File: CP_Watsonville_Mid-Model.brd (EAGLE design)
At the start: 100 x 100 mm, 12 parts

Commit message: Aligned between boards
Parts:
- moved CON1 3.81 mm to (88.9, 21.6)
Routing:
- net DAAT: track 91.9 -> 96.0 mm
- net 1SAAT: track 79.9 -> 83.9 mm
- net 2SAAT: track 68.9 -> 72.9 mm
- net 3SAAT: track 58.1 -> 62.1 mm
- net 4SAAT: track 47.1 -> 51.1 mm
- net VCC: track 152.0 -> 155.8 mm
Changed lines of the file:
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@@
 <layer number="19" name="Unrouted" color="6" fill="1" visible="no" active="yes"/>
 <layer number="20" name="Dimension" color="15" fill="1" visible="yes" active="yes"/>
-<layer number="21" name="tPlace" color="7" fill="1" visible="yes" active="yes"/>
+<layer number="21" name="tPlace" color="39" fill="1" visible="yes" active="yes"/>
 <layer number="22" name="bPlace" color="7" fill="1" visible="no" active="yes"/>
 <layer number="23" name="tOrigins" color="15" fill="1" visible="no" active="yes"/>
@@
 <text x="48.514" y="41.783" size="1.27" layer="21" font="vector" ratio="10">3SAAT</text>
 <text x="48.514" y="29.083" size="1.27" layer="21" font="vector" ratio="10">4SAAT</text>
-<text x="76.327" y="23.241" size="1.016" layer="21" font="vector" ratio="10">John Plocher</text>
-<text x="77.597" y="20.701" size="1.016" layer="21" font="vector" ratio="10">2020.10</text>
+<text x="84.709" y="12.192" size="1.016" layer="22" font="vector" ratio="10" rot="MR90">John Plocher</text>
+<text x="82.169" y="13.462" size="1.016" layer="22" font="vector" ratio="10" rot="MR90">2020.10</text>
 <text x="92.456" y="82.042" size="5.08" layer="22" font="vector" ratio="15" rot="MR0">SPCoast.com
 CP Watsonville Middle</text>
 <text x="85.09" y="48.26" size="5.08" layer="22" font="vector" ratio="15" rot="MR0">Model Board
 Field Unit repeater</text>
-<text x="91.44" y="7.62" size="2.54" layer="22" font="vector" ratio="10" rot="MR0">V1.0 2020.10</text>
+<text x="60.96" y="2.54" size="2.54" layer="22" font="vector" ratio="10" rot="MR0">V1.0 2020.10</text>
 <text x="5.08" y="77.47" size="2.54" layer="22" font="vector" ratio="10" rot="MR270">Model Railroading is Fun!</text>
 <text x="97.79" y="90.17" size="2.54" layer="22" font="vector" ratio="10" rot="MR270">Made in the PCR, Coast Division, NMRA</text>
@@
 <wire x1="97.79" y1="33.02" x2="95.25" y2="33.02" width="0.6096" layer="21"/>
 <wire x1="1.27" y1="83.82" x2="3.81" y2="83.82" width="0.6096" layer="21"/>
-<circle x="88.9" y="25.4" radius="1.79605" width="0.4064" layer="21"/>
+<circle x="88.9" y="21.59" radius="1.79605" width="0.4064" layer="22"/>
 </plain>
 <attributes>
@@
 <attribute name="VALUE" x="52.07" y="34.925" size="0.3048" layer="27" font="vector" rot="R180"/>
 </element>
-<element name="CON1" library="SPCoast" package="1X06_LOCK" value="" x="88.9" y="25.4" rot="R270"/>
+<element name="CON1" library="SPCoast" package="1X06_LOCK" value="" x="88.9" y="21.59" rot="R270"/>
 </elements>
 <signals>
@@
 <wire x1="49.9" y1="58.42" x2="49.9" y2="45.72" width="0.3048" layer="1"/>
 <wire x1="49.9" y1="45.72" x2="49.9" y2="33.02" width="0.3048" layer="1"/>
-<wire x1="88.9" y1="25.4" x2="88.9" y2="85.09" width="0.4064" layer="1"/>
+<wire x1="88.9" y1="21.59" x2="88.9" y2="85.09" width="0.4064" layer="1"/>
 <wire x1="88.9" y1="85.09" x2="87.63" y2="86.36" width="0.4064" layer="1"/>
 <wire x1="87.63" y1="86.36" x2="50.8" y2="86.36" width="0.4064" layer="1"/>
@@
 <wire x1="55.36" y1="45.72" x2="78.74" y2="45.72" width="0.3048" layer="1"/>
 <wire x1="78.74" y1="45.72" x2="80.01" y2="44.45" width="0.3048" layer="1"/>
-<wire x1="80.01" y1="44.45" x2="80.01" y2="24.13" width="0.3048" layer="1"/>
-<wire x1="80.01" y1="24.13" x2="88.9" y2="15.24" width="0.3048" layer="1"/>
+<wire x1="80.01" y1="44.45" x2="80.01" y2="19.685" width="0.3048" layer="1"/>
+<wire x1="80.01" y1="19.685" x2="88.9" y2="11.43" width="0.3048" layer="1"/>
 </signal>
 <signal name="2SAAT">
@@
 <wire x1="55.36" y1="58.42" x2="80.01" y2="58.42" width="0.3048" layer="1"/>
 <wire x1="80.01" y1="58.42" x2="81.28" y2="57.15" width="0.3048" layer="1"/>
-<wire x1="81.28" y1="57.15" x2="81.28" y2="25.146" width="0.3048" layer="1"/>
-<wire x1="81.28" y1="25.146" x2="88.646" y2="17.78" width="0.3048" layer="1"/>
+<wire x1="81.28" y1="57.15" x2="81.28" y2="20.701" width="0.3048" layer="1"/>
+<wire x1="81.28" y1="20.701" x2="88.646" y2="13.97" width="0.3048" layer="1"/>
 </signal>
 <signal name="4SAAT">
@@
 <wire x1="55.36" y1="33.02" x2="77.47" y2="33.02" width="0.3048" layer="1"/>
 <wire x1="77.47" y1="33.02" x2="78.74" y2="31.75" width="0.3048" layer="1"/>
-<wire x1="78.74" y1="31.75" x2="78.74" y2="22.606" width="0.3048" layer="1"/>
-<wire x1="78.74" y1="22.606" x2="88.646" y2="12.7" width="0.3048" layer="1"/>
+<wire x1="78.74" y1="31.75" x2="78.74" y2="18.161" width="0.3048" layer="1"/>
+<wire x1="78.74" y1="18.161" x2="88.646" y2="8.89" width="0.3048" layer="1"/>
 </signal>
 <signal name="N$26">
@@
 <wire x1="54.09" y1="83.82" x2="82.55" y2="83.82" width="0.3048" layer="1"/>
 <wire x1="82.55" y1="83.82" x2="83.82" y2="82.55" width="0.3048" layer="1"/>
-<wire x1="83.82" y1="82.55" x2="83.82" y2="27.686" width="0.3048" layer="1"/>
-<wire x1="83.82" y1="27.686" x2="88.646" y2="22.86" width="0.3048" layer="1"/>
+<wire x1="83.82" y1="82.55" x2="83.82" y2="23.241" width="0.3048" layer="1"/>
+<wire x1="83.82" y1="23.241" x2="88.646" y2="19.05" width="0.3048" layer="1"/>
 </signal>
 <signal name="1SAAT">
@@
 <wire x1="55.36" y1="71.12" x2="81.28" y2="71.12" width="0.3048" layer="1"/>
 <wire x1="81.28" y1="71.12" x2="82.55" y2="69.85" width="0.3048" layer="1"/>
-<wire x1="82.55" y1="69.85" x2="82.55" y2="26.67" width="0.3048" layer="1"/>
-<wire x1="82.55" y1="26.67" x2="88.9" y2="20.32" width="0.3048" layer="1"/>
+<wire x1="82.55" y1="69.85" x2="82.55" y2="22.225" width="0.3048" layer="1"/>
+<wire x1="82.55" y1="22.225" x2="88.9" y2="16.51" width="0.3048" layer="1"/>
 </signal>
 </signals>

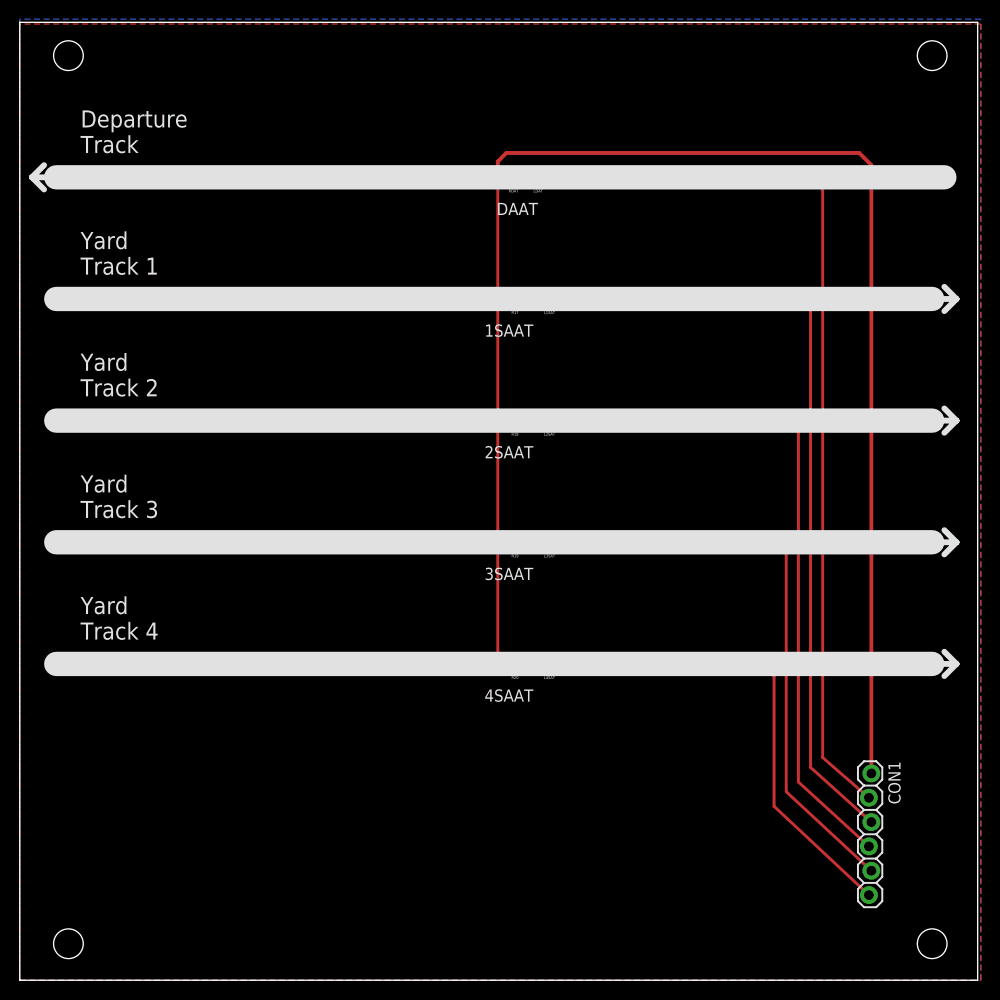
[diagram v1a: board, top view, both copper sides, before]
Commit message: Round corner board
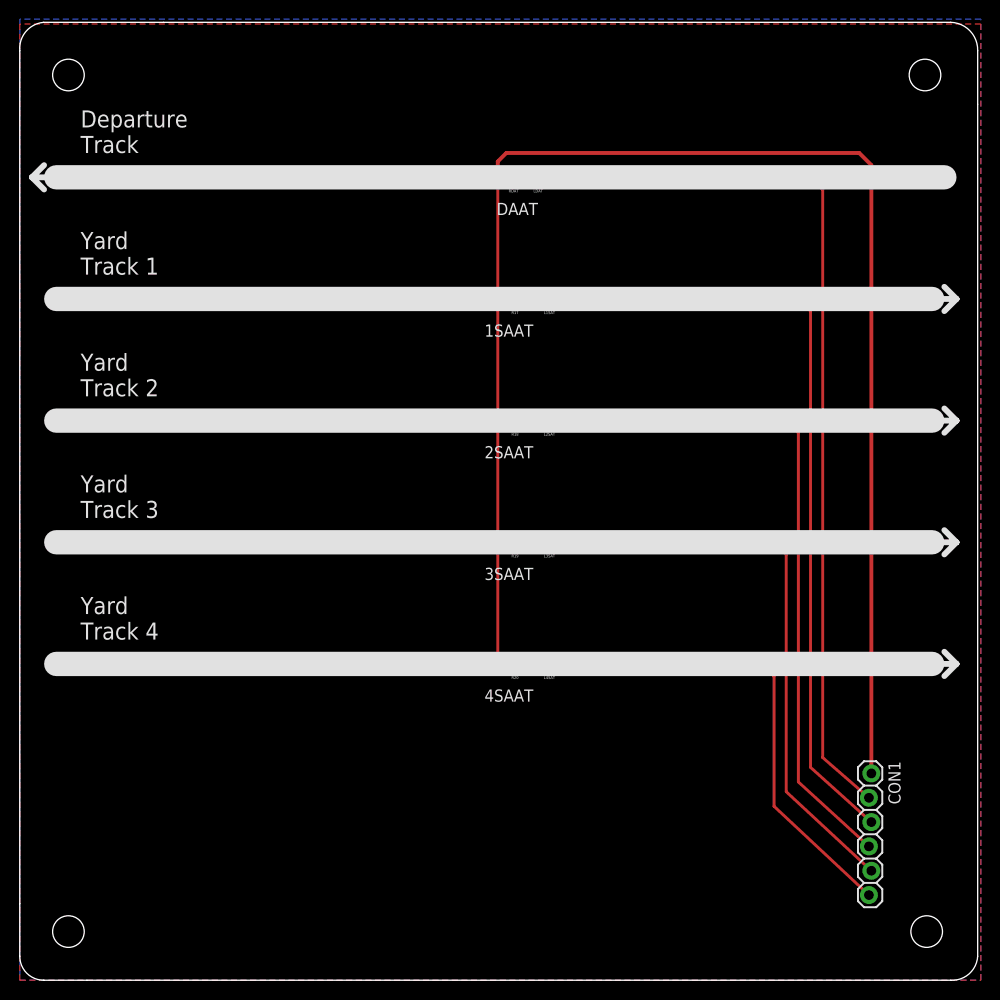
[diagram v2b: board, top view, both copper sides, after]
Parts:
- BOARD1: device SPCoast:BOARD-10X10-TEMPLATE -> SPCoast:BOARD-SEEED10X10
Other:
- outline, holes or cut-outs redrawn
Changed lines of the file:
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@@
 <grid distance="50" unitdist="mil" unit="mil" style="dots" multiple="2" display="yes" altdistance="25" altunitdist="mil" altunit="mil"/>
 <layers>
-<layer number="1" name="Top" color="4" fill="1" visible="no" active="yes"/>
+<layer number="1" name="Top" color="4" fill="1" visible="yes" active="yes"/>
 <layer number="2" name="Route2" color="1" fill="3" visible="no" active="no"/>
 <layer number="3" name="Route3" color="4" fill="3" visible="no" active="no"/>
 <layer number="14" name="Route14" color="1" fill="6" visible="no" active="no"/>
 <layer number="15" name="Route15" color="4" fill="6" visible="no" active="no"/>
-<layer number="16" name="Bottom" color="1" fill="1" visible="no" active="yes"/>
+<layer number="16" name="Bottom" color="1" fill="1" visible="yes" active="yes"/>
 <layer number="17" name="Pads" color="2" fill="1" visible="yes" active="yes"/>
 <layer number="18" name="Vias" color="2" fill="1" visible="yes" active="yes"/>
-<layer number="19" name="Unrouted" color="6" fill="1" visible="no" active="yes"/>
+<layer number="19" name="Unrouted" color="6" fill="1" visible="yes" active="yes"/>
 <layer number="20" name="Dimension" color="15" fill="1" visible="yes" active="yes"/>
 <layer number="21" name="tPlace" color="39" fill="1" visible="yes" active="yes"/>
 <layer number="22" name="bPlace" color="7" fill="1" visible="no" active="yes"/>
-<layer number="23" name="tOrigins" color="15" fill="1" visible="no" active="yes"/>
+<layer number="23" name="tOrigins" color="15" fill="1" visible="yes" active="yes"/>
 <layer number="24" name="bOrigins" color="15" fill="1" visible="no" active="yes"/>
-<layer number="25" name="tNames" color="7" fill="1" visible="no" active="yes"/>
+<layer number="25" name="tNames" color="7" fill="1" visible="yes" active="yes"/>
 <layer number="26" name="bNames" color="7" fill="1" visible="no" active="yes"/>
 <layer number="27" name="tValues" color="7" fill="1" visible="yes" active="yes"/>
@@
 <layer number="42" name="bRestrict" color="1" fill="10" visible="no" active="yes"/>
 <layer number="43" name="vRestrict" color="2" fill="10" visible="no" active="yes"/>
-<layer number="44" name="Drills" color="7" fill="1" visible="no" active="yes"/>
-<layer number="45" name="Holes" color="7" fill="1" visible="no" active="yes"/>
-<layer number="46" name="Milling" color="3" fill="1" visible="no" active="yes"/>
-<layer number="47" name="Measures" color="7" fill="1" visible="no" active="yes"/>
+<layer number="44" name="Drills" color="7" fill="1" visible="yes" active="yes"/>
+<layer number="45" name="Holes" color="7" fill="1" visible="yes" active="yes"/>
+<layer number="46" name="Milling" color="3" fill="1" visible="yes" active="yes"/>
+<layer number="47" name="Measures" color="7" fill="1" visible="yes" active="yes"/>
 <layer number="48" name="Document" color="7" fill="1" visible="yes" active="yes"/>
-<layer number="49" name="Reference" color="7" fill="1" visible="no" active="yes"/>
+<layer number="49" name="Reference" color="7" fill="1" visible="yes" active="yes"/>
 <layer number="50" name="dxf" color="7" fill="1" visible="no" active="no"/>
 <layer number="51" name="tDocu" color="7" fill="1" visible="yes" active="yes"/>
@@
 <layer number="99" name="Anatomie" color="7" fill="1" visible="no" active="no"/>
 <layer number="100" name="Muster" color="7" fill="1" visible="no" active="no"/>
-<layer number="101" name="Hidden" color="57" fill="4" visible="no" active="yes"/>
-<layer number="102" name="Changes" color="13" fill="1" visible="no" active="yes"/>
+<layer number="101" name="Hidden" color="57" fill="4" visible="yes" active="yes"/>
+<layer number="102" name="Changes" color="13" fill="1" visible="yes" active="yes"/>
 <layer number="103" name="tMap" color="29" fill="4" visible="no" active="yes"/>
-<layer number="104" name="Name" color="16" fill="1" visible="no" active="yes"/>
+<layer number="104" name="Name" color="16" fill="1" visible="yes" active="yes"/>
 <layer number="105" name="tPlate" color="7" fill="1" visible="no" active="yes"/>
 <layer number="106" name="bPlate" color="7" fill="1" visible="no" active="yes"/>
@@
 </autorouter>
 <elements>
-<element name="BOARD1" library="SPCoast" package="BOARD-10X10-TEMPLATE" value="" x="0" y="0" smashed="yes"/>
+<element name="BOARD1" library="SPCoast" package="BOARD-SEEED10X10" value="" x="0" y="0" smashed="yes"/>
 <element name="LDAT" library="SPCoast" package="0603-LED" value="Y" x="53.34" y="83.82" smashed="yes" rot="R180">
 <attribute name="NAME" x="54.61" y="82.55" size="0.3048" layer="25" rot="R180"/>
